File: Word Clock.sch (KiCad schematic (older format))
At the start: 0 parts

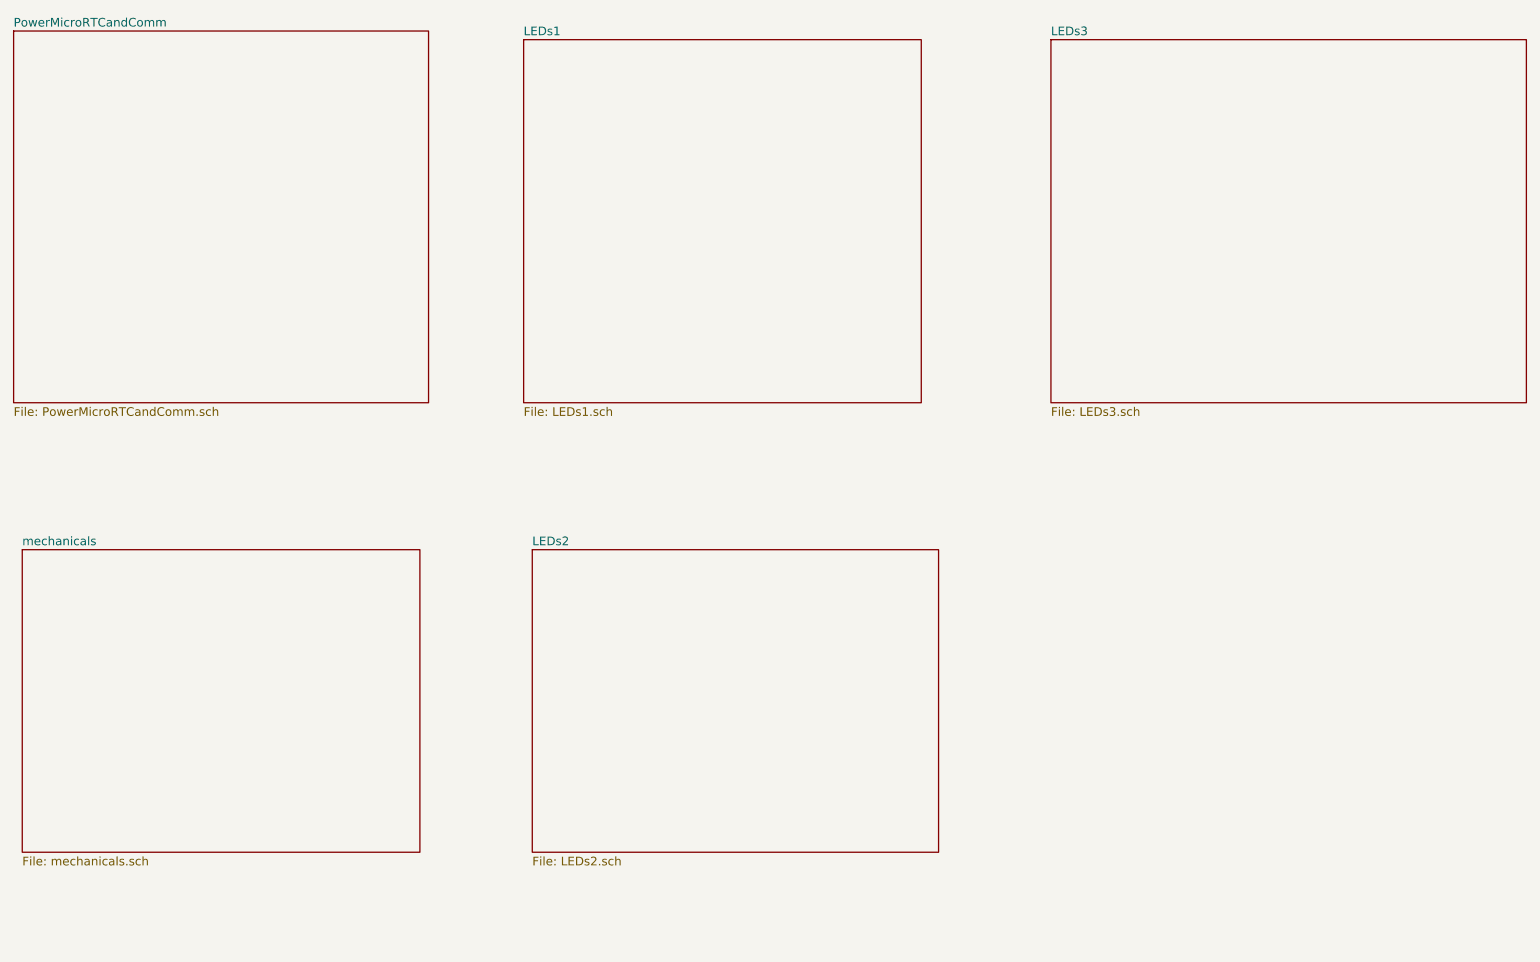
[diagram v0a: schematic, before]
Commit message: Schematic is almost finished. The MCLR circuit needs completing, the hour/minute inputs also need their input protection.
After that, I might have one of the guys from work review it. But, who knows.
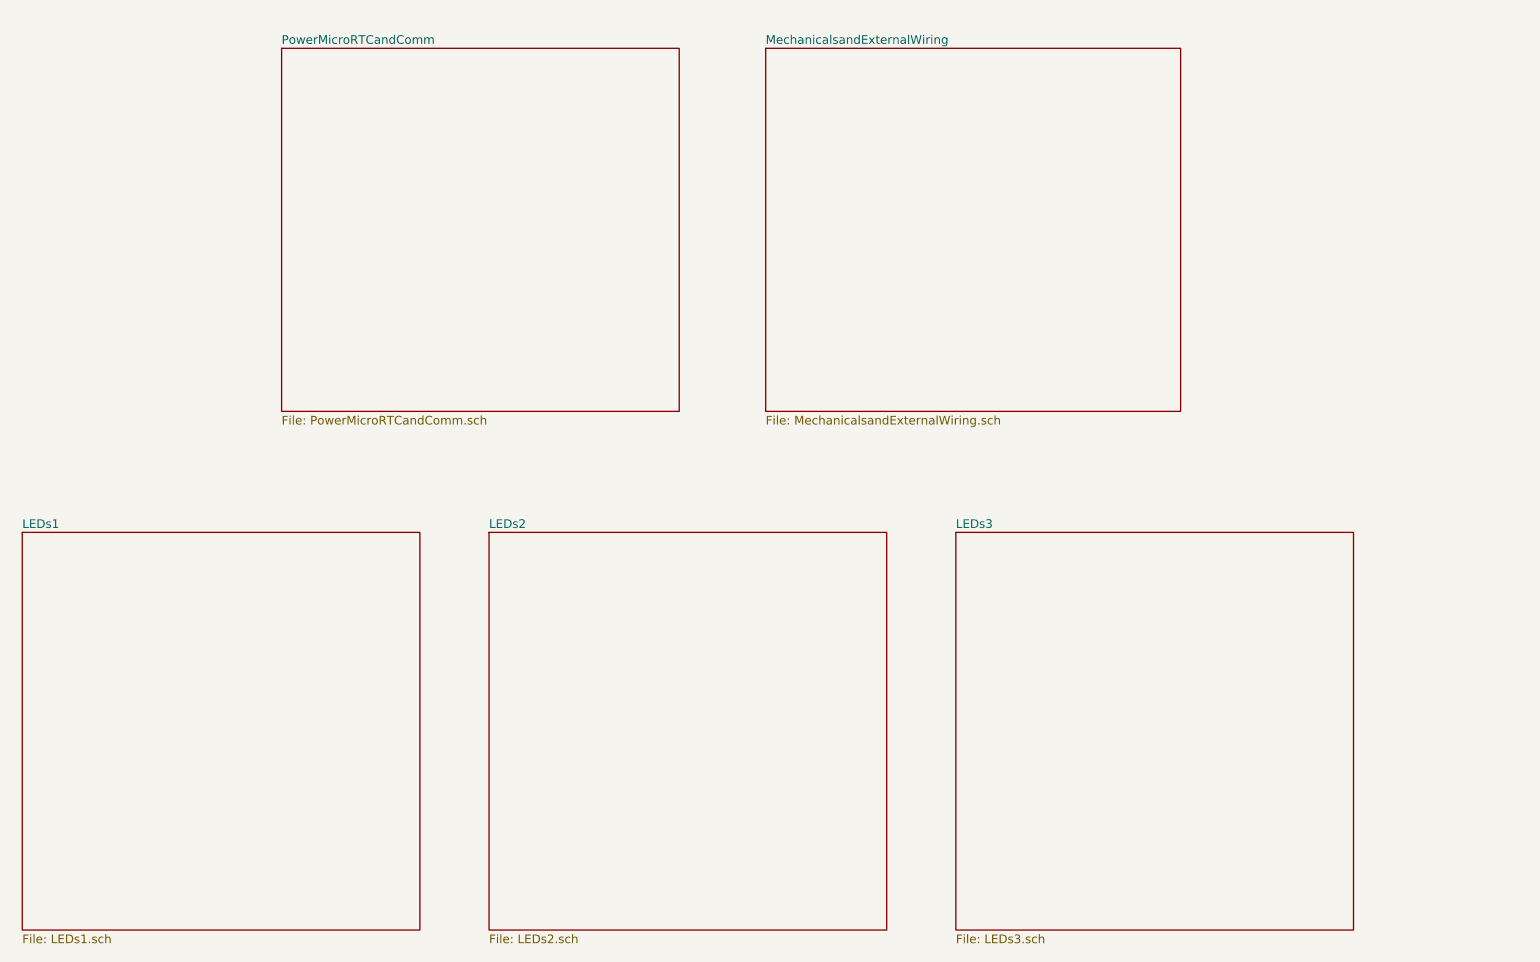
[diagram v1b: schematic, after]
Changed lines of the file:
@@
 $EndDescr
 $Sheet
-S 1250 1100 2400 2150
+S 2800 1200 2300 2100
 U 601A8FF2
 F0 "PowerMicroRTCandComm" 50
@@
 $EndSheet
 $Sheet
-S 4200 1150 2300 2100
+S 1300 4000 2300 2300
 U 601A911C
 F0 "LEDs1" 50
@@
 $EndSheet
 $Sheet
-S 1300 4100 2300 1750
-U 602D3479
-F0 "mechanicals" 50
-F1 "mechanicals.sch" 50
-$EndSheet
-$Sheet
-S 4250 4100 2350 1750
+S 4000 4000 2300 2300
 U 603C2CB1
 F0 "LEDs2" 50
@@
 $EndSheet
 $Sheet
-S 7250 1150 2750 2100
+S 6700 4000 2300 2300
 U 60490D00
 F0 "LEDs3" 50
 F1 "LEDs3.sch" 50
 $EndSheet
+$Sheet
+S 5600 1200 2400 2100
+U 602D3479
+F0 "MechanicalsandExternalWiring" 50
+F1 "MechanicalsandExternalWiring.sch" 50
+$EndSheet
 $EndSCHEMATC
